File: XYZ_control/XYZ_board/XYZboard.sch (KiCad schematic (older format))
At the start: 79 parts, among them J1 DB9_connector, J10 Control_1, J11 Sensor_1, J12 Settings_2, J13 Control_2, J14 Sensor_2, J15 Settings_3, J16 Control_3, J17 Sensor_3, J2 DB9_connector, J3 DB9_connector, J4 PWR IN, J5 Settings_1, U1 A4988_stepper_driver, U2 A4988_stepper_driver, U3 A4988_stepper_driver, U4 LM317MSTT3G_Voltage_Regulator

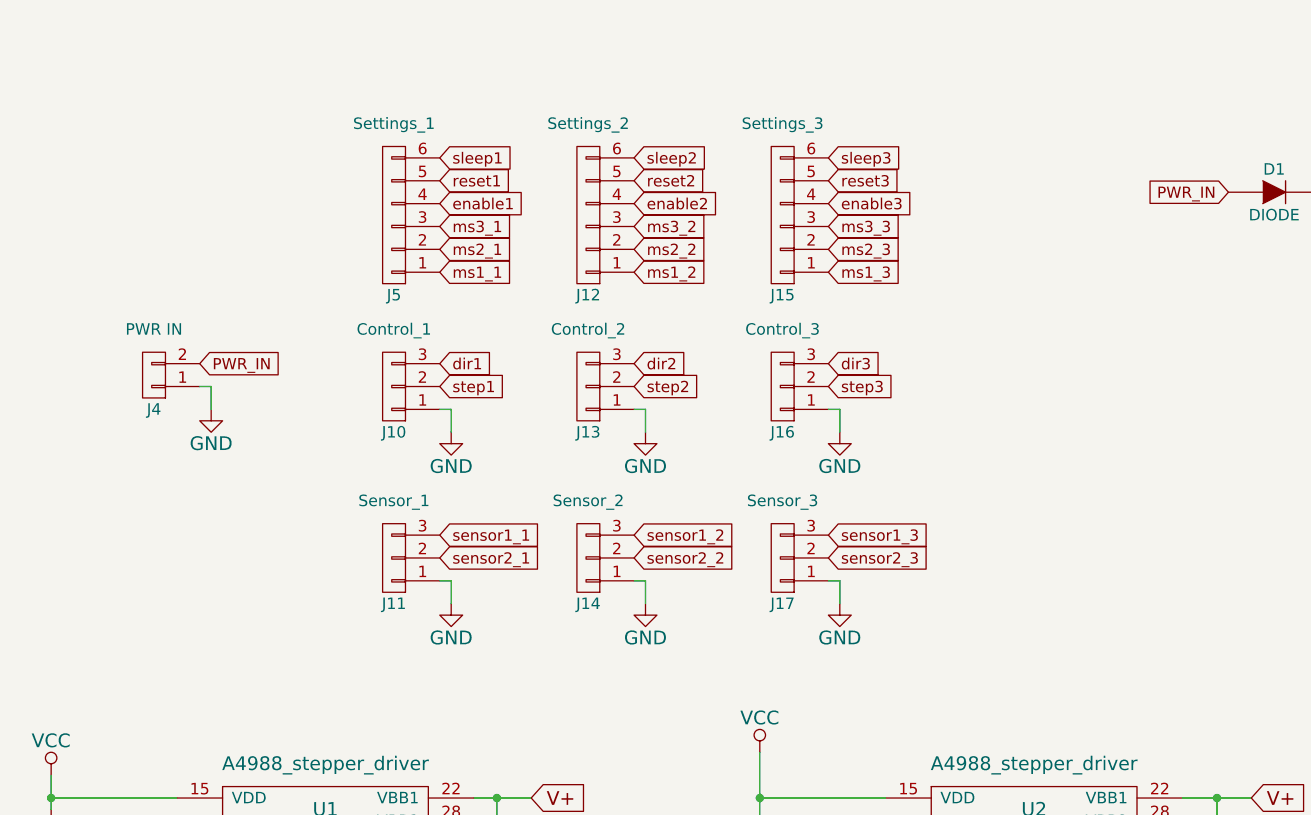
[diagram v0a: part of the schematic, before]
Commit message: Updated motor control board
Added pull up resistors for the hall effect sensors
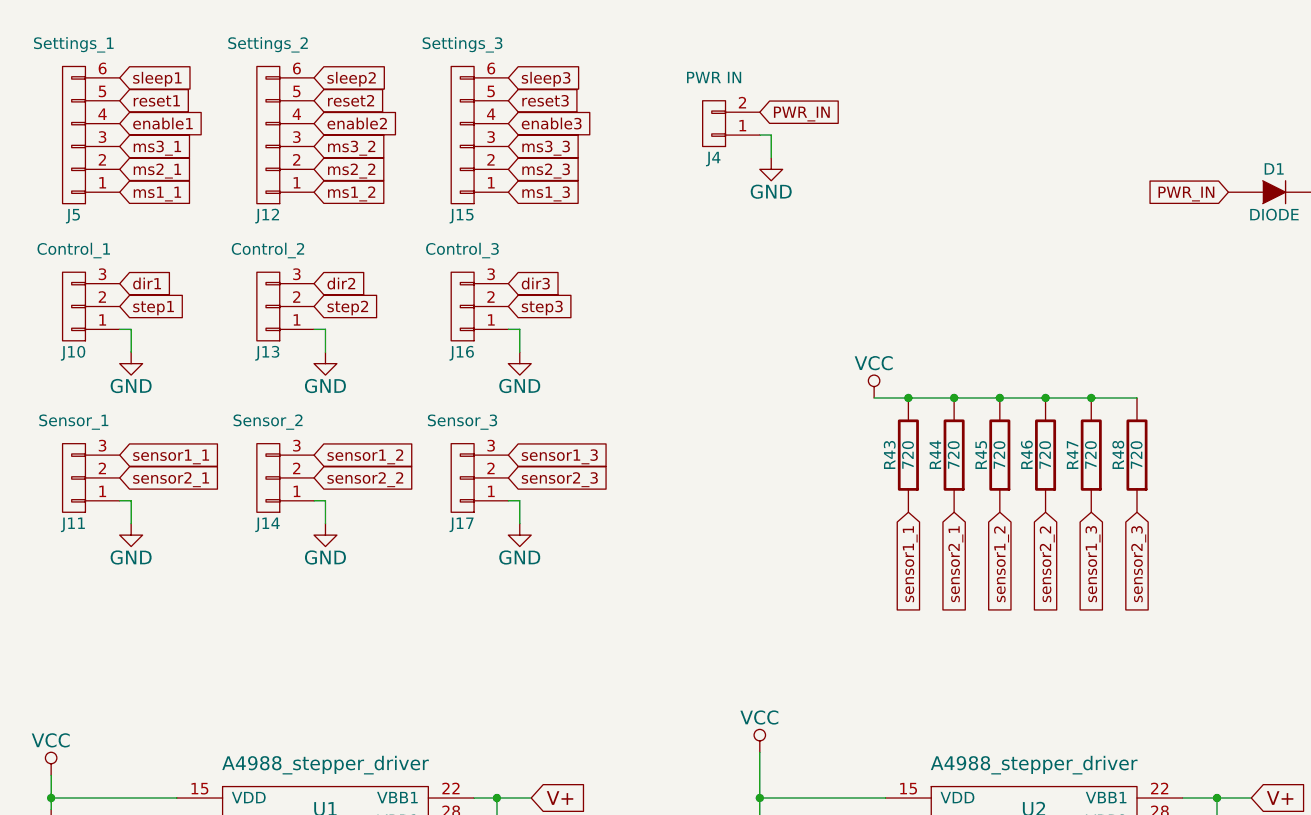
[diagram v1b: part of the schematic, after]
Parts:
- added R43, R44, R45, R46, R47, R48: 720, Resistors_SMD:R_0603_HandSoldering, symbol R
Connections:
- net VCC: now also R43.2, R44.2, R45.2, R46.2, R47.2, R48.2
- net sensor1_1: now also R43.1
- net sensor1_2: now also R45.1
- net sensor1_3: now also R47.1
- net sensor2_1: now also R44.1
- net sensor2_2: now also R46.1
- net sensor2_3: now also R48.1
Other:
- moved on the sheet: J10, J11, J12, J13, J14, J15, J16, J17, J4, J5

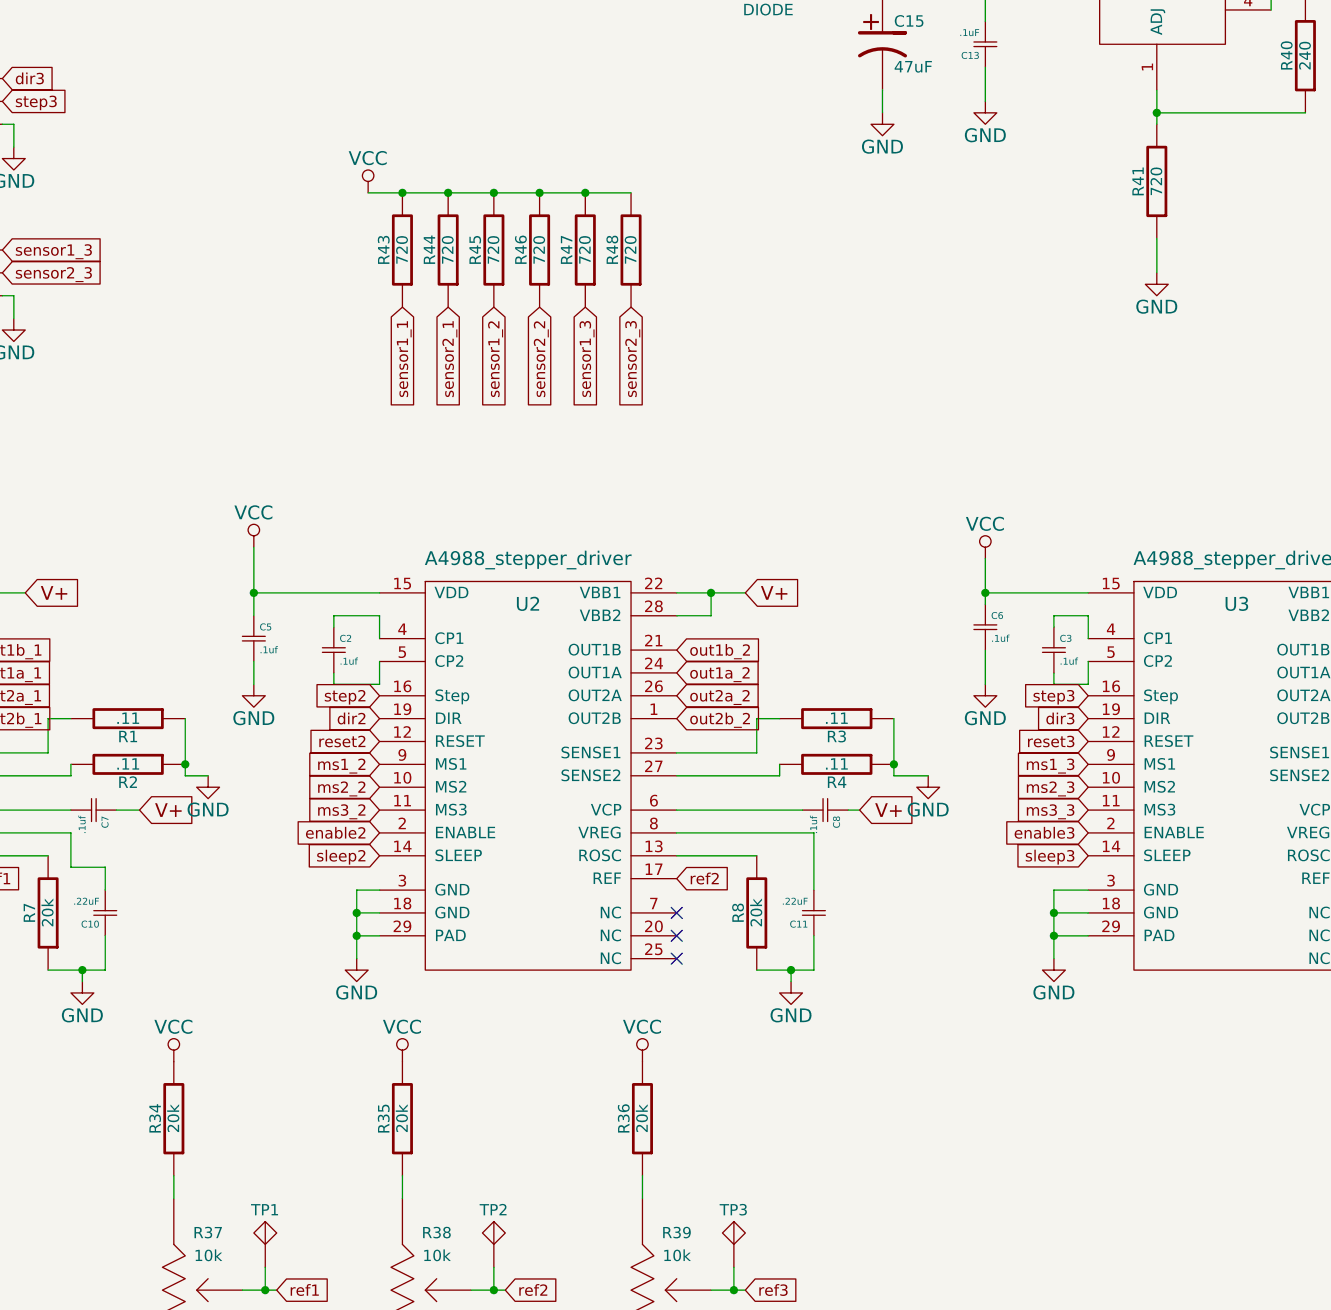
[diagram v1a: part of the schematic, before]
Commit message: updated resistor values
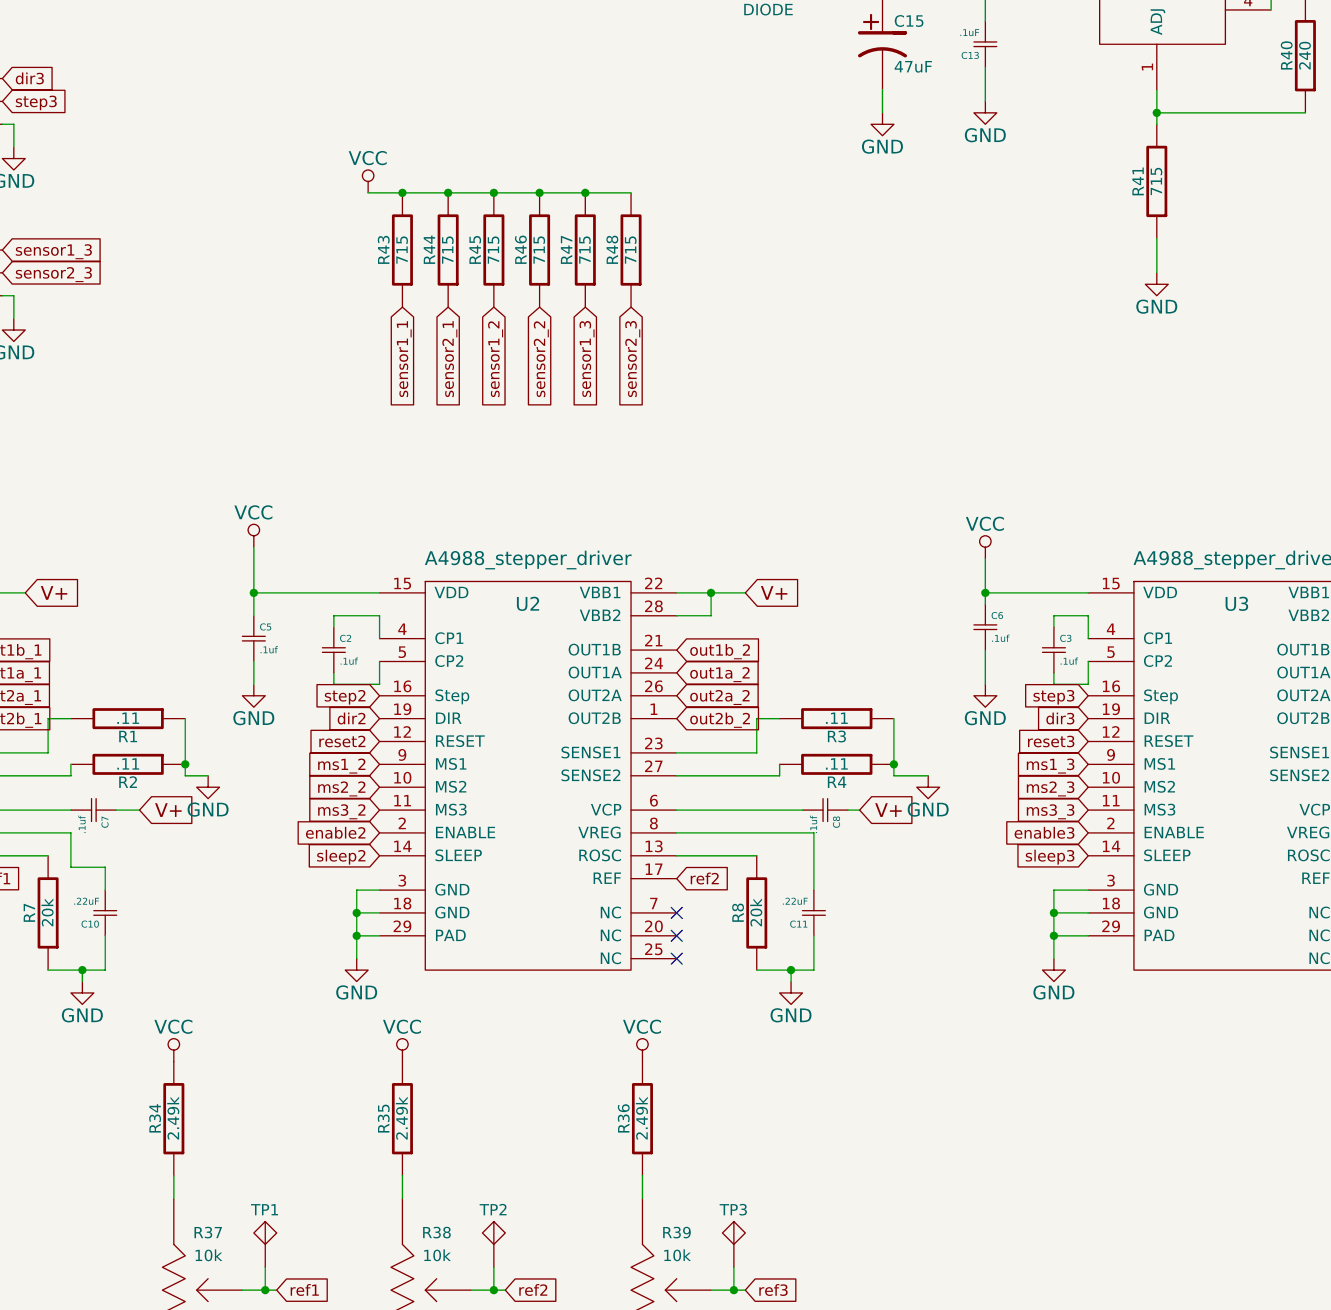
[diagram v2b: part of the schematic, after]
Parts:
- R34, R35, R36: value 20k -> 2.49k
- R41, R43, R44, R45, R46, R47, R48: value 720 -> 715
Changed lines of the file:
@@
 P 3500 6250
 F 0 "R34" V 3580 6250 50  0000 C CNN
-F 1 "20k" V 3500 6250 50  0000 C CNN
+F 1 "2.49k" V 3500 6250 50  0000 C CNN
 F 2 "" V 3430 6250 30  0001 C CNN
 F 3 "" H 3500 6250 30  0000 C CNN
@@
 P 4500 6250
 F 0 "R35" V 4580 6250 50  0000 C CNN
-F 1 "20k" V 4500 6250 50  0000 C CNN
+F 1 "2.49k" V 4500 6250 50  0000 C CNN
 F 2 "" V 4430 6250 30  0001 C CNN
 F 3 "" H 4500 6250 30  0000 C CNN
@@
 P 5550 6250
 F 0 "R36" V 5630 6250 50  0000 C CNN
-F 1 "20k" V 5550 6250 50  0000 C CNN
+F 1 "2.49k" V 5550 6250 50  0000 C CNN
 F 2 "" V 5480 6250 30  0001 C CNN
 F 3 "" H 5550 6250 30  0000 C CNN
@@
 P 7800 2150
 F 0 "R41" V 7880 2150 50  0000 C CNN
-F 1 "720" V 7800 2150 50  0000 C CNN
+F 1 "715" V 7800 2150 50  0000 C CNN
 F 2 "" V 7730 2150 30  0001 C CNN
 F 3 "" H 7800 2150 30  0000 C CNN
@@
 P 4500 2450
 F 0 "R43" V 4580 2450 50  0000 C CNN
-F 1 "720" V 4500 2450 50  0000 C CNN
+F 1 "715" V 4500 2450 50  0000 C CNN
 F 2 "Resistors_SMD:R_0603_HandSoldering" V 4430 2450 30  0001 C CNN
 F 3 "" H 4500 2450 30  0000 C CNN
@@
 P 4700 2450
 F 0 "R44" V 4780 2450 50  0000 C CNN
-F 1 "720" V 4700 2450 50  0000 C CNN
+F 1 "715" V 4700 2450 50  0000 C CNN
 F 2 "Resistors_SMD:R_0603_HandSoldering" V 4630 2450 30  0001 C CNN
 F 3 "" H 4700 2450 30  0000 C CNN
@@
 P 4900 2450
 F 0 "R45" V 4980 2450 50  0000 C CNN
-F 1 "720" V 4900 2450 50  0000 C CNN
+F 1 "715" V 4900 2450 50  0000 C CNN
 F 2 "Resistors_SMD:R_0603_HandSoldering" V 4830 2450 30  0001 C CNN
 F 3 "" H 4900 2450 30  0000 C CNN
@@
 P 5100 2450
 F 0 "R46" V 5180 2450 50  0000 C CNN
-F 1 "720" V 5100 2450 50  0000 C CNN
+F 1 "715" V 5100 2450 50  0000 C CNN
 F 2 "Resistors_SMD:R_0603_HandSoldering" V 5030 2450 30  0001 C CNN
 F 3 "" H 5100 2450 30  0000 C CNN
@@
 P 5300 2450
 F 0 "R47" V 5380 2450 50  0000 C CNN
-F 1 "720" V 5300 2450 50  0000 C CNN
+F 1 "715" V 5300 2450 50  0000 C CNN
 F 2 "Resistors_SMD:R_0603_HandSoldering" V 5230 2450 30  0001 C CNN
 F 3 "" H 5300 2450 30  0000 C CNN
@@
 P 5500 2450
 F 0 "R48" V 5580 2450 50  0000 C CNN
-F 1 "720" V 5500 2450 50  0000 C CNN
+F 1 "715" V 5500 2450 50  0000 C CNN
 F 2 "Resistors_SMD:R_0603_HandSoldering" V 5430 2450 30  0001 C CNN
 F 3 "" H 5500 2450 30  0000 C CNN

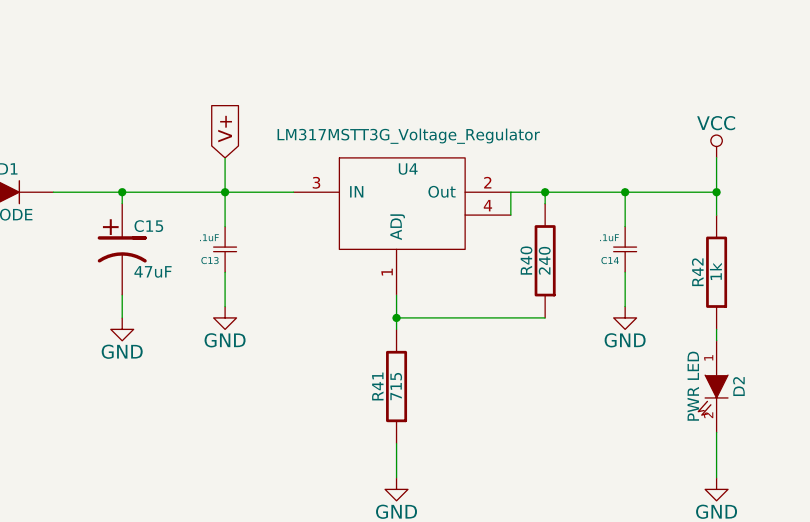
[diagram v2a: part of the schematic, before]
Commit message: Updated parts on board
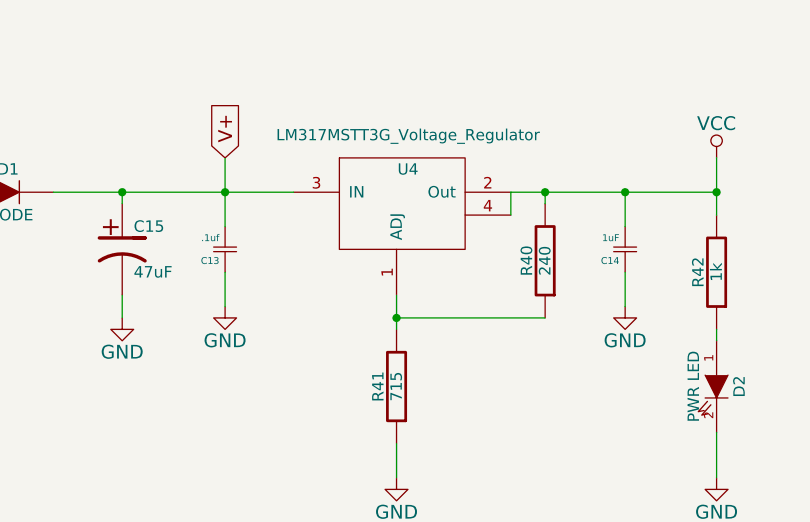
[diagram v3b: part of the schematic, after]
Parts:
- C13: value .1uF -> .1uf
- C14: value .1uF -> 1uF
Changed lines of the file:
@@
 P 7050 1550
 F 0 "C13" H 7075 1600 30  0000 L CNN
-F 1 ".1uF" H 7075 1500 30  0000 L CNN
+F 1 ".1uf" H 7075 1500 30  0000 L CNN
 F 2 "" H 7050 1550 60  0001 C CNN
 F 3 "" H 7050 1550 60  0000 C CNN
@@
 P 8800 1550
 F 0 "C14" H 8825 1600 30  0000 L CNN
-F 1 ".1uF" H 8825 1500 30  0000 L CNN
+F 1 "1uF" H 8825 1500 30  0000 L CNN
 F 2 "" H 8800 1550 60  0001 C CNN
 F 3 "" H 8800 1550 60  0000 C CNN
